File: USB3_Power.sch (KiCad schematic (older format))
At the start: 53 parts

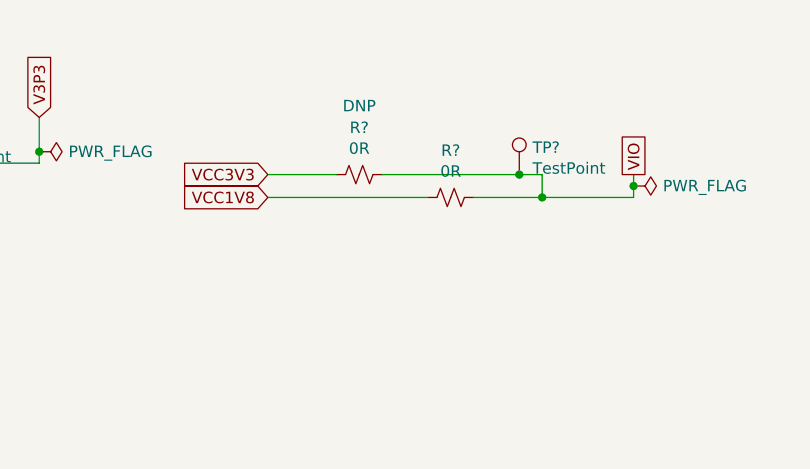
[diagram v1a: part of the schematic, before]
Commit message: Added nets for fx3 usb3 cct from fpga
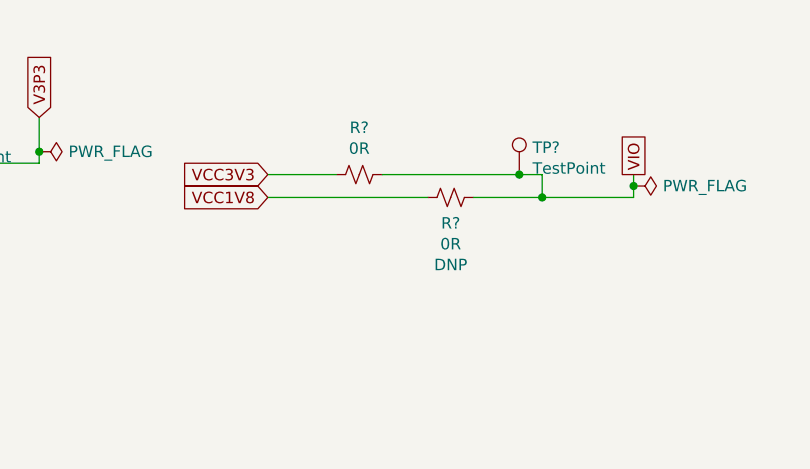
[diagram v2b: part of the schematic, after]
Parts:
- R?: DNP (none) -> DNP
- R?: DNP DNP -> (none)
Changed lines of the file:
@@
 $Descr A4 11693 8268
 encoding utf-8
-Sheet 8 22
+Sheet 14 22
 Title ""
 Date ""
@@
 U 1 1 603D73B3
 P 5150 1450
-F 0 "R?" V 4945 1450 50  0000 C CNN
-F 1 "0R" V 5036 1450 50  0000 C CNN
+F 0 "R?" V 5263 1450 50  0000 C CNN
+F 1 "0R" V 5354 1450 50  0000 C CNN
 F 2 "Resistor_SMD:R_0603_1608Metric_Pad0.98x0.95mm_HandSolder" H 5150 1450 50  0001 C CNN
 F 3 "~" H 5150 1450 50  0001 C CNN
-F 4 "" V 5150 1450 50  0001 C CNN "DNP"
+F 4 "DNP" V 5445 1450 50  0000 C CNN "DNP"
 	1    5150 1450
 	0    1    1    0
@@
 F 2 "Resistor_SMD:R_0603_1608Metric_Pad0.98x0.95mm_HandSolder" H 4750 1350 50  0001 C CNN
 F 3 "~" H 4750 1350 50  0001 C CNN
-F 4 "DNP" V 4450 1350 50  0000 C CNN "DNP"
 	1    4750 1350
 	0    1    1    0

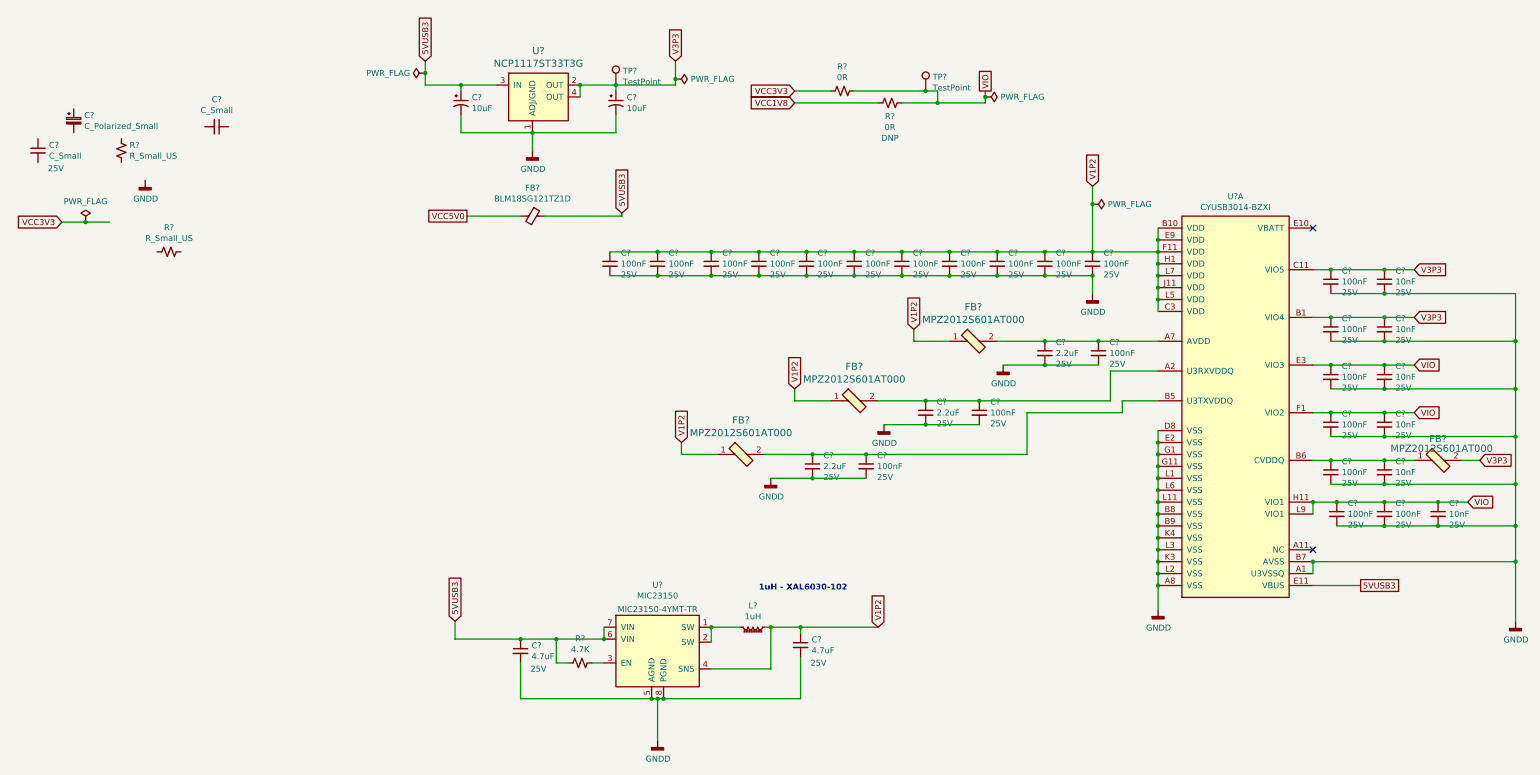
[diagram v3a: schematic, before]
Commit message: PCB created and schematics annotated High speed connections added to the BTB
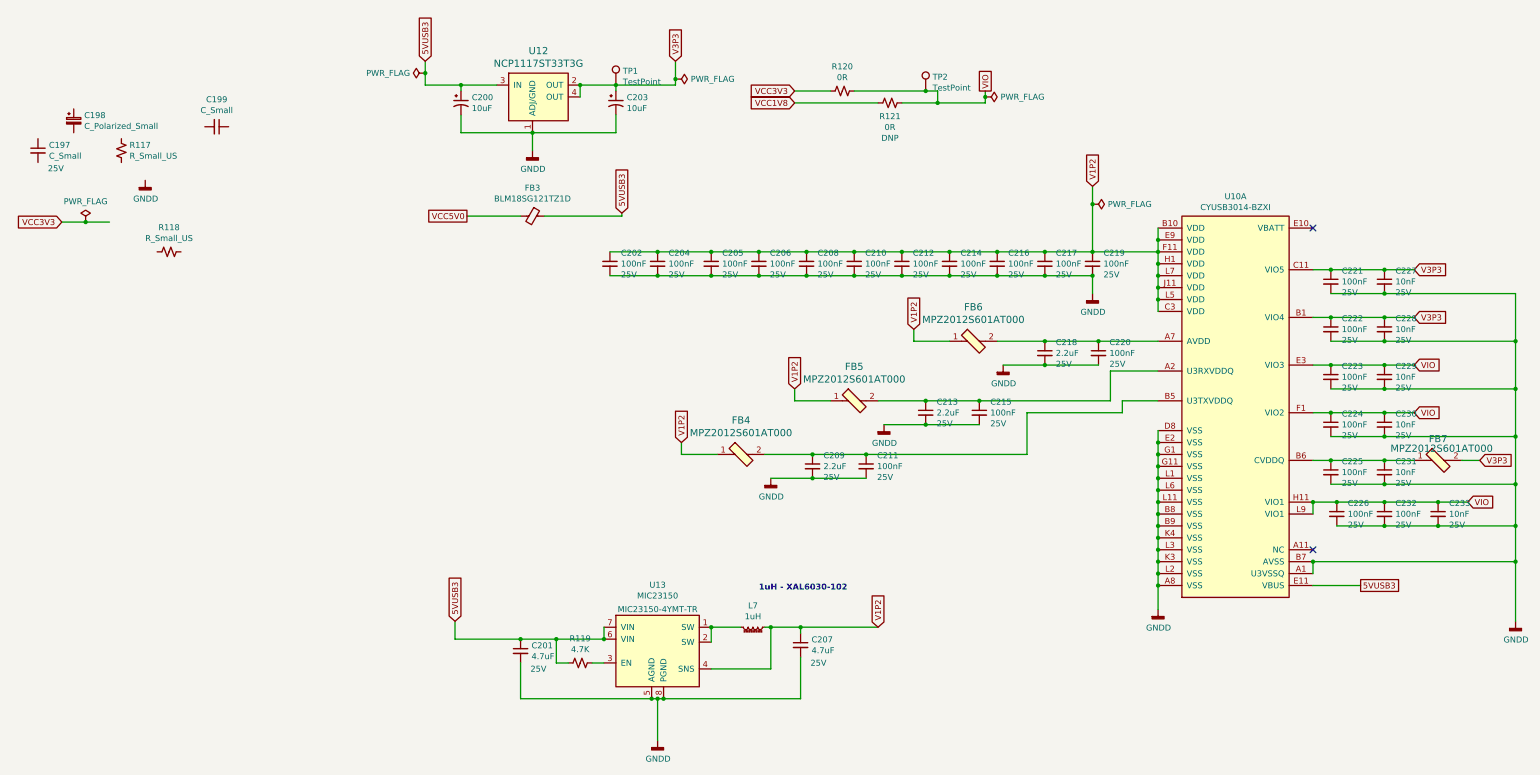
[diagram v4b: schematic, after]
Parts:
- gave numbers to parts that had none: 53

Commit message: Corrected PCB import errors
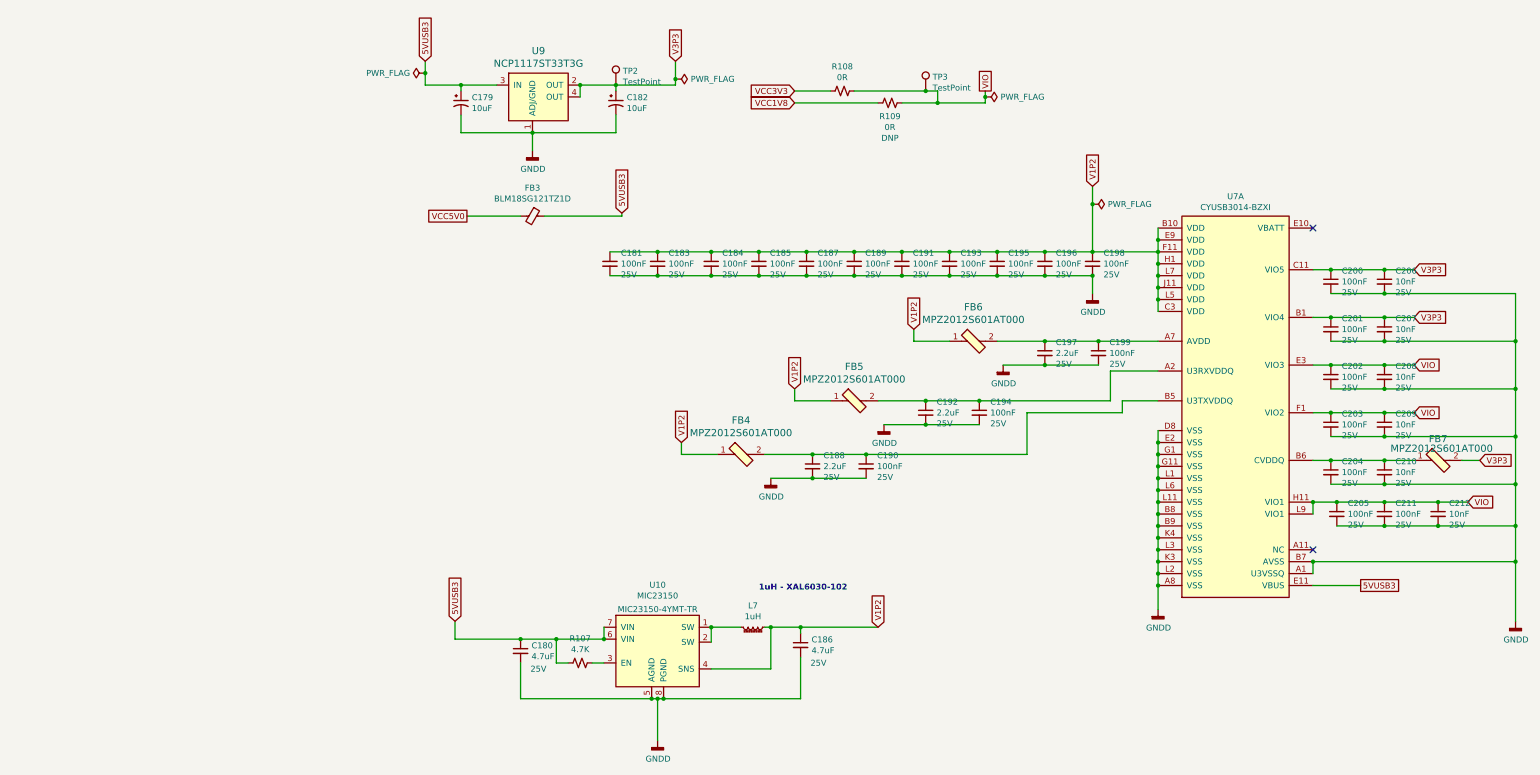
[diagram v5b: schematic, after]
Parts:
- removed C197: C_Small, Capacitor_SMD:C_0603_1608Metric_Pad1.08x0.95mm_HandSolder, symbol Device:C_Small
- removed C198: C_Polarized_Small, Capacitor_Tantalum_SMD:CP_EIA-1608-10_AVX-L_Pad1.25x1.05mm_HandSolder, symbol Device:C_Polarized_Small
- removed C199: C_Small, symbol Device:C_Small
- removed R117, R118: R_Small_US, Resistor_SMD:R_0603_1608Metric_Pad0.98x0.95mm_HandSolder, symbol Device:R_Small_US
- L7: footprint (none) -> Inductor_SMD:L_Coilcraft_XAL60xx_6.36x6.56mm
- renumbered C200 to C179, C201 to C180, C202 to C181, C203 to C182, C204 to C183, C205 to C184, C206 to C185, C207 to C186, C208 to C187, C209 to C188, C210 to C189, C211 to C190, C212 to C191, C213 to C192, C214 to C193, C215 to C194, C216 to C195, C217 to C196, C218 to C197, C219 to C198, C220 to C199, C221 to C200, C222 to C201, C223 to C202, C224 to C203, C225 to C204, C226 to C205, C227 to C206, C228 to C207, C229 to C208, C230 to C209, C231 to C210, C232 to C211, C233 to C212, R119 to R107, R120 to R108, R121 to R109, TP1 to TP2, TP2 to TP3, U13 to U10, U10 to U7, U12 to U9
